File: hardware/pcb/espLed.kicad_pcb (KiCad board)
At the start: 2 copper layers, 32.3 x 36.6 mm, 23 parts, among them J1 led_strip, J2 flashing, J3 power, Q1 IRF9310TRPBF, Q2 AO3400A, Q3 AO3400A, Q4 AO3400A, SW1 reset, SW2 flash, U1 AMS1117-3.3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

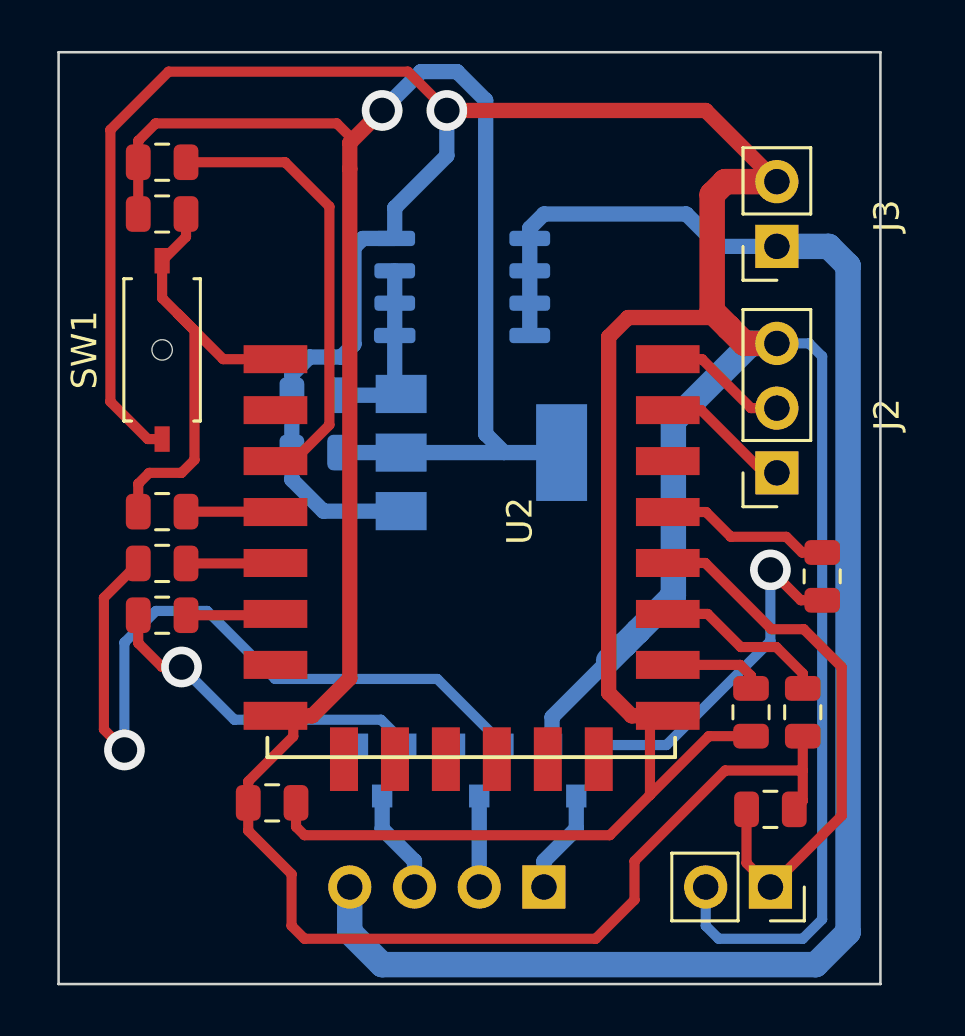
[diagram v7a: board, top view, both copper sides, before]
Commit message: rewire two transistors' GNDs neater
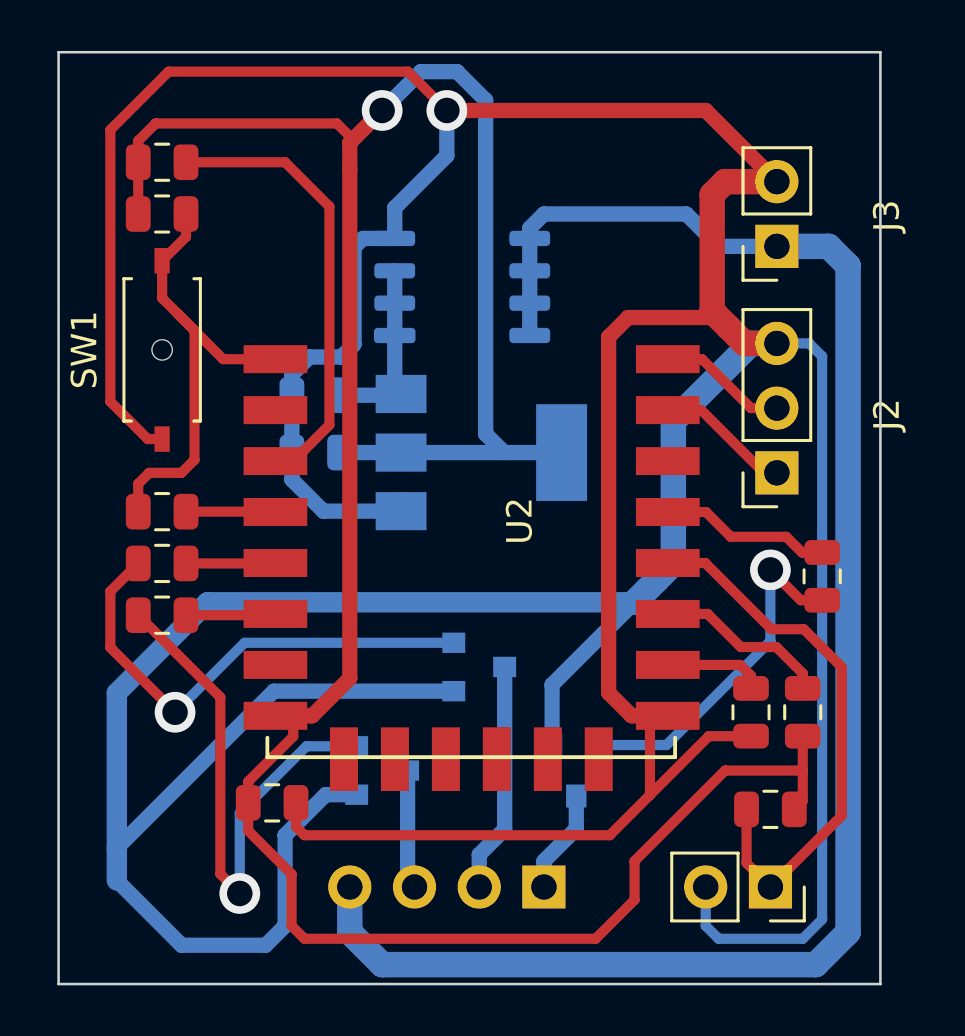
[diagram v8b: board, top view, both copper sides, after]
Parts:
- moved Q3 4.06 mm to (179.6, 130.3), turned to 0 degrees
- turned Q4 to 0 degrees
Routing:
- net GND: track 175.1 -> 233.4 mm
- net Net-(Q3-Pad2): track 30.0 -> 19.4 mm
- net Net-(Q4-Pad2): track 13.3 -> 21.4 mm
- net /led2_out: track 3.57 -> 9.05 mm
- net /led3_out: track 4.10 -> 4.68 mm
